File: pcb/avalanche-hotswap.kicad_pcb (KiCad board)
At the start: 2 copper layers, 179.7 x 122.7 mm, 138 parts, among them J1 TRRS, J2 OLED, P1 i2c_pin, P2 i2c_pin, P3 battery+, P4 battery-, SW0 SW_Push, SW1 SW_Push, SW10 SW_Push, SW11 SW_Push, SW12 SW_Push, SW13 SW_Push, SW14 SW_Push, SW15 SW_Push, SW16 SW_Push, SW17 SW_Push, SW18 SW_Push, SW19 SW_Push, SW2 SW_Push, SW20 SW_Push, SW21 SW_Push, SW22 SW_Push, SW23 SW_Push, SW24 SW_Push, SW25 SW_Push, SW26 SW_Push, SW27 SW_Push, SW28 SW_Push, SW29 SW_Push, SW3 SW_Push, SW30 SW_Push, SW31 SW_Push, SW32 SW_Push, SW33 SW_DPDT_x2, SW34 SW_DPDT_x2, SW4 SW_Push, SW5 SW_Push, SW6 SW_Push, SW7 SW_Push, SW8 SW_Push, SW9 SW_Push, U1 ProMicro

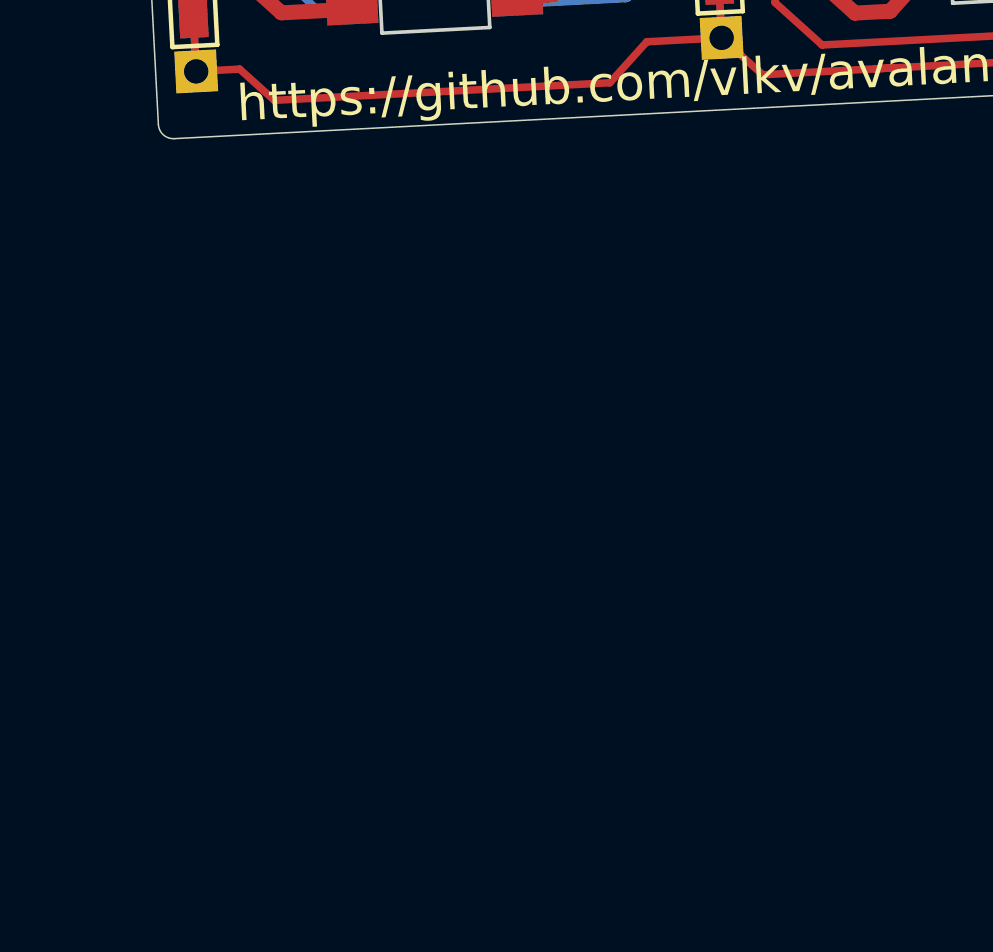
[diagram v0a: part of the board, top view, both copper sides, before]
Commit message: Modifications to have the palm key.
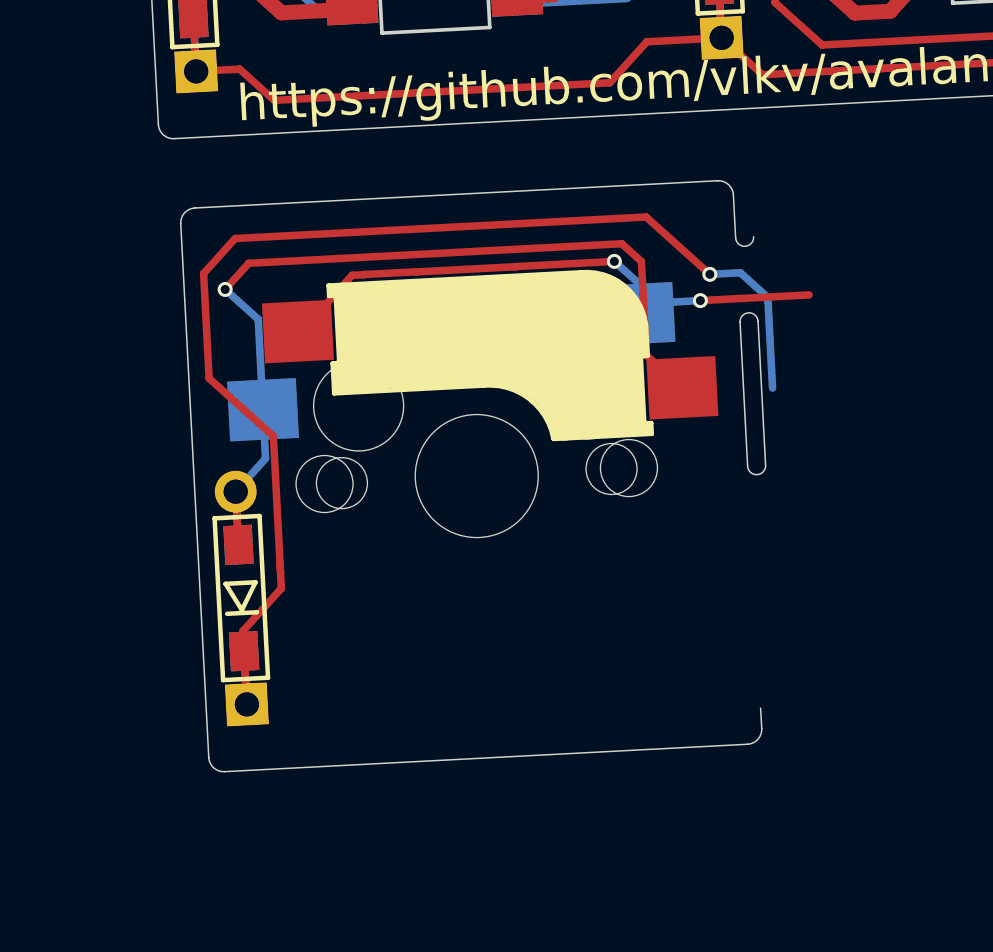
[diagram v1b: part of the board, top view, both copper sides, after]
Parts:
- added D27: 1N4148, used_footprints:diode_TH_SMD, F.Cu at (84.3, 125.8)
- added SW27: SW_Push, used_footprints:CherryMX_MidHeight_Hotswap_1u, F.Cu at (92.2, 121.7)
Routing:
- net (no net): track 0.09 -> 91.5 mm, vias 0 -> 4
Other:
- outline, holes or cut-outs redrawn
